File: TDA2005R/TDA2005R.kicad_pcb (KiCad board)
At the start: 2 copper layers, 71.1 x 71.1 mm, 26 parts, among them J1 6-pole_dual_potentiometer_hea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, U1 4-pole_RL-input_screw_terminal, U2 TDA2005, U3 4-pole_RL-output_screw_termin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, U4 2-pole_power_in_screw_terminal

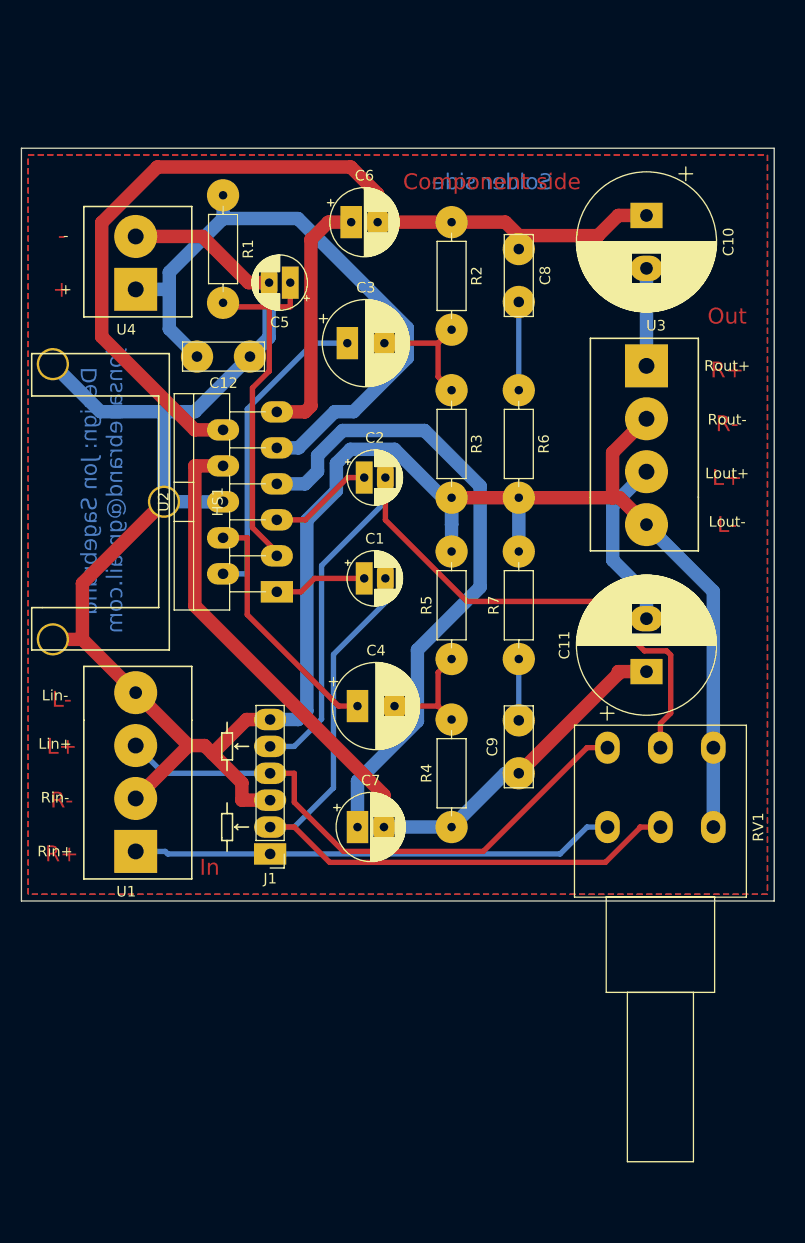
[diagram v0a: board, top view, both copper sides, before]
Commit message: wider tracks and text
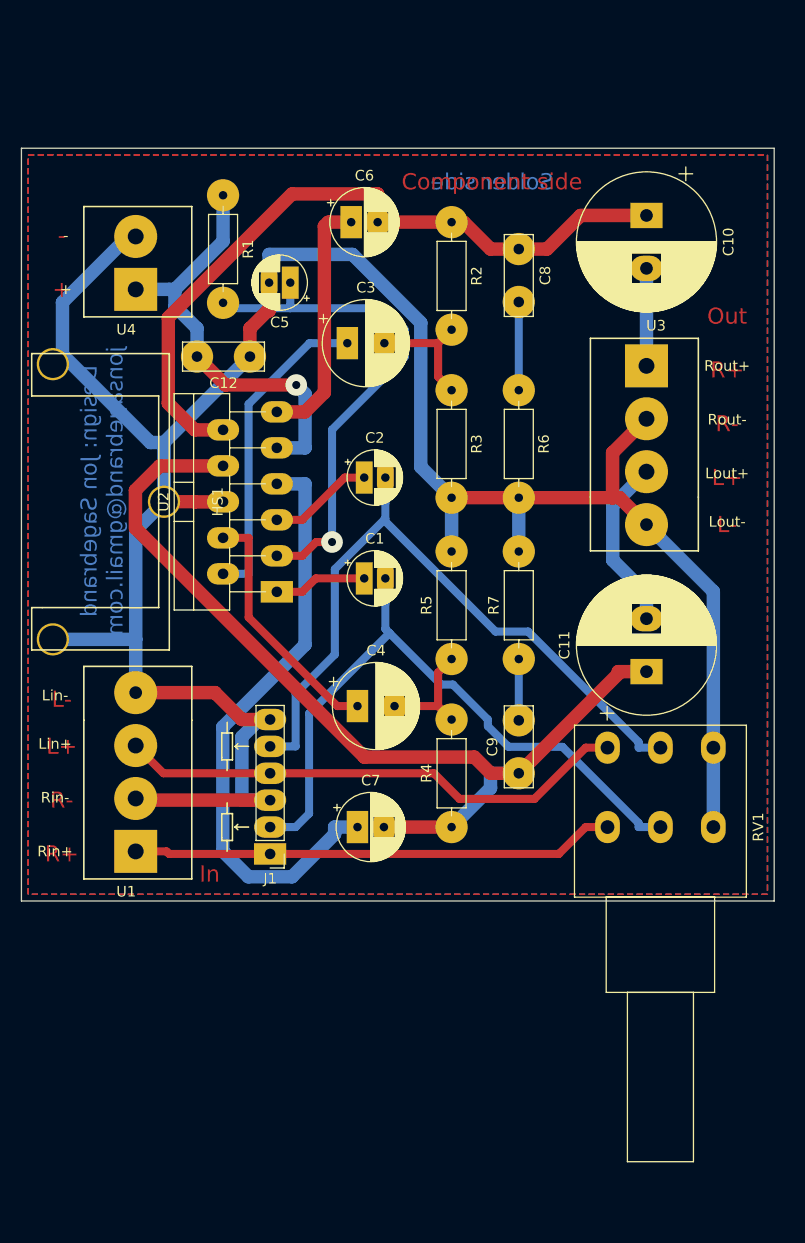
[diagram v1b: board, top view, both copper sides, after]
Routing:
- net +15V: track 62.0 -> 41.1 mm, vias 0 -> 1
- net Net-(C10-Pad1): track 85.8 -> 69.4 mm
- net Net-(C5-Pad1): track 33.9 -> 49.3 mm, vias 0 -> 1
- net Net-(C11-Pad1): track 75.2 -> 90.5 mm
- net Net-(C2-Pad2): track 76.7 -> 66.7 mm
- net Lin: track 54.4 -> 48.7 mm
- net Net-(C1-Pad2): track 69.0 -> 63.5 mm
- net Net-(C7-Pad1): track 61.4 -> 56.7 mm
- net GND: track 230.0 -> 231.7 mm
- added copper zone on B.Cu, net (none)
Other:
- net class 20 removed
- net class 30: via_dia 1.27 -> 2.032
- net class Default: via_dia 0.8 -> 3.048; via_drill 0.4 -> 0.762

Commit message: new component sizes
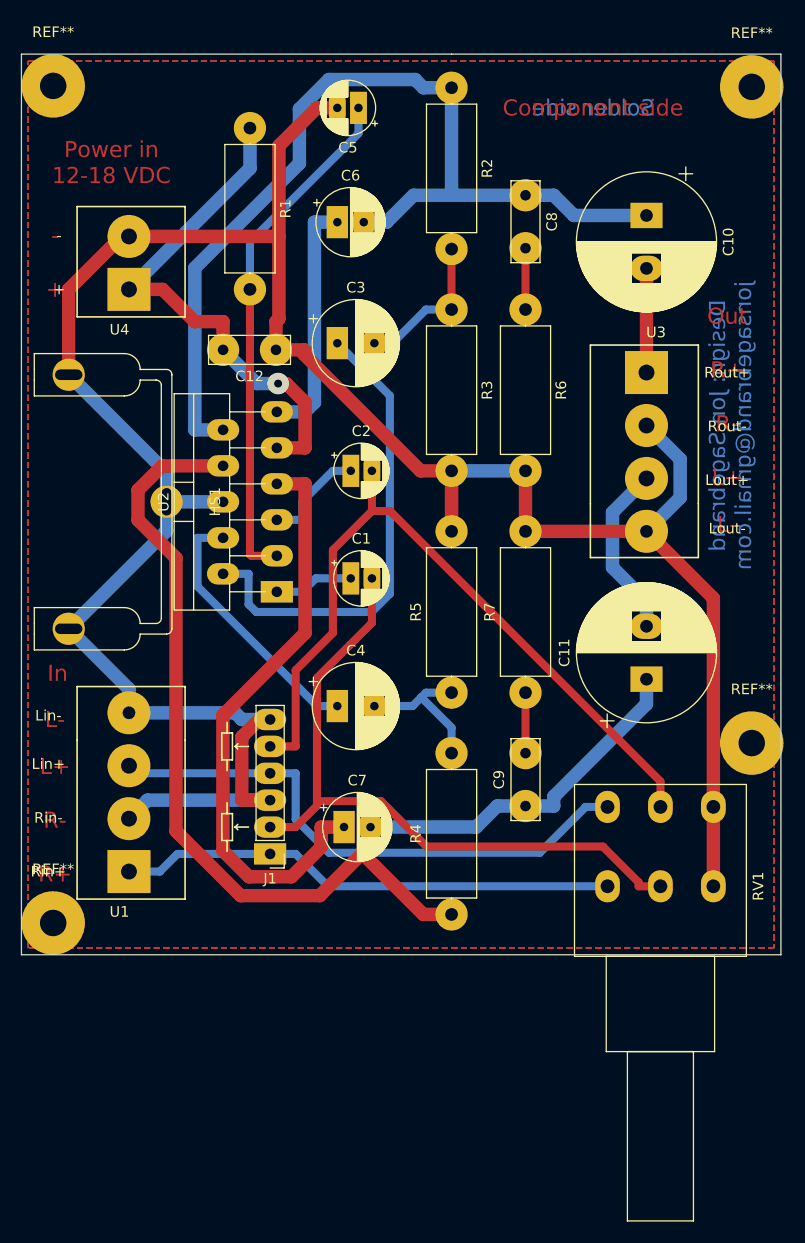
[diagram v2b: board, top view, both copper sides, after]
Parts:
- added REF**: SolderWirePad_1x01_Drill2.5mm, Connector_Wire:SolderWirePad_1x01_Drill2.5mm, F.Cu at (206.2, 119.7)
- added REF**: SolderWirePad_1x01_Drill2.5mm, Connector_Wire:SolderWirePad_1x01_Drill2.5mm, F.Cu at (206.2, 57.7)
- added REF**: SolderWirePad_1x01_Drill2.5mm, Connector_Wire:SolderWirePad_1x01_Drill2.5mm, F.Cu at (140.2, 136.7)
- added REF**: SolderWirePad_1x01_Drill2.5mm, Connector_Wire:SolderWirePad_1x01_Drill2.5mm, F.Cu at (140.2, 57.6)
- R1, R2, R3, R4, R5, R6, R7: footprint My_Misc:R_Axial_DIN0207_L6.3mm_D2.5mm_P10.16mm_Horizontal_larger_pads -> My_Misc:R_Axial_DIN0414_L11.9mm_D4.5mm_P15.24mm_Horizontal_larger
- moved C5 17.7 mm to (169.0, 59.7)
- moved R2 12.7 mm to (177.8, 57.8)
- moved R4 8.25 mm to (177.8, 135.9)
- moved R6 7.65 mm to (184.8, 78.7)
- moved R3 7.62 mm to (177.8, 78.7)
- moved R1 6.84 mm to (158.8, 61.6)
- moved RV1 5.59 mm to (192.5, 133.2)
- moved C8 5.12 mm to (184.8, 67.9)
- moved R7 3.24 mm to (184.8, 114.9)
- moved R5 3.17 mm to (177.8, 114.9)
- moved C9 3.16 mm to (184.8, 125.7)
- moved C12 2.54 mm to (161.2, 82.5)
- moved U1 2.01 mm to (147.3, 131.8)
- moved C4 1.91 mm to (167.0, 116.2)
- moved C2 1.42 mm to (168.3, 94.0)
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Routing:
- net Net-(C10-Pad1): track 69.4 -> 91.6 mm
- net Net-(C11-Pad1): track 90.5 -> 111.9 mm
- net Net-(C3-Pad1): track 30.2 -> 45.4 mm
- net GND: track 231.7 -> 243.6 mm
- net +15V: track 41.1 -> 49.6 mm
- net Net-(C2-Pad2): track 66.7 -> 71.7 mm
- net Lin: track 48.7 -> 53.0 mm
- net Net-(C4-Pad2): track 10.9 -> 14.3 mm
- net Net-(C3-Pad2): track 11.8 -> 14.4 mm
- net Net-(C8-Pad2): track 8.33 -> 5.80 mm
- net Rin: track 45.7 -> 47.2 mm
- net Net-(C1-Pad2): track 63.5 -> 64.9 mm
- net Net-(C1-Pad1): track 8.78 -> 7.51 mm
- net Net-(C4-Pad1): track 23.7 -> 24.9 mm
- net Rout: track 9.21 -> 9.84 mm
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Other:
- board size 71.1 x 71.1 mm -> 71.8 x 85.1 mm
- board text added: "Power in 12-18 VDC"

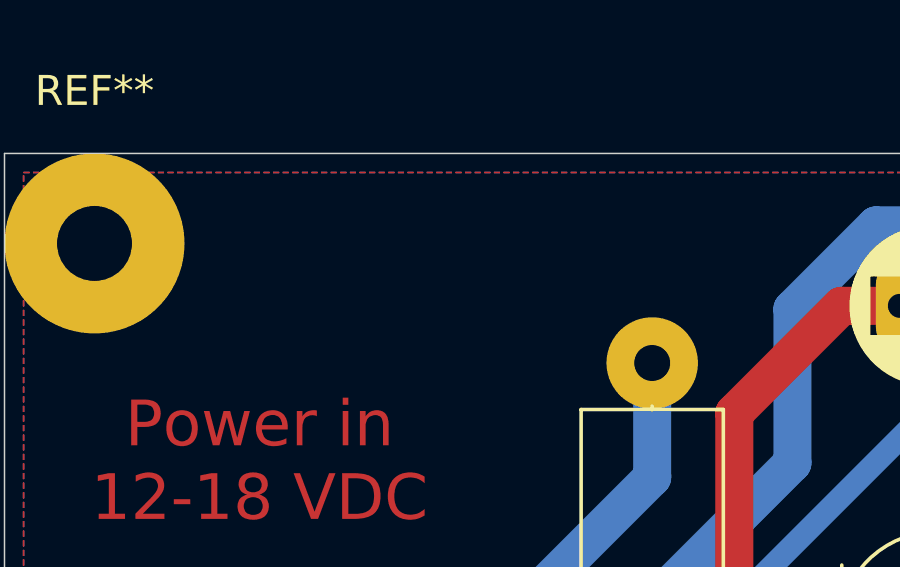
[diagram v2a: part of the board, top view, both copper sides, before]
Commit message: new resistors, new heatsink
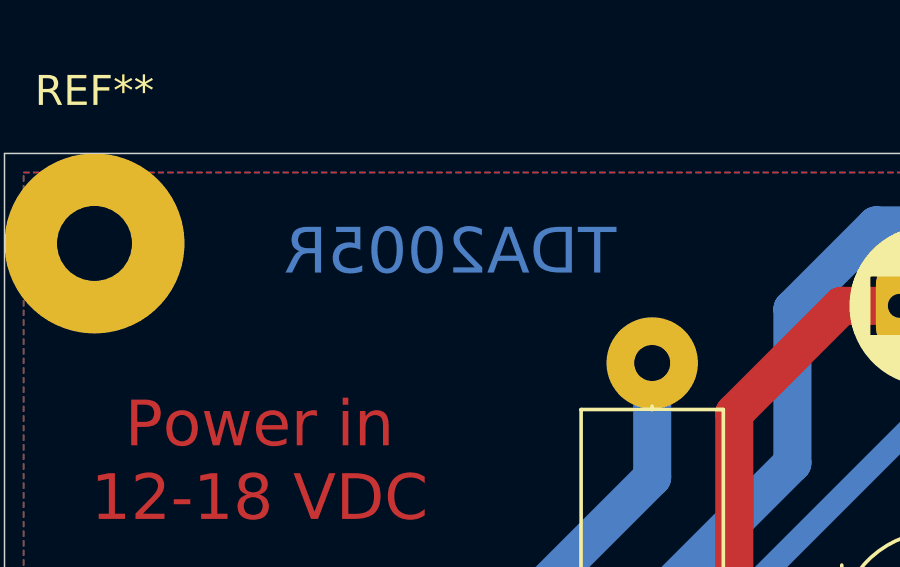
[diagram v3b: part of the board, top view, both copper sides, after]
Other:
- board text added: "TDA2005R"
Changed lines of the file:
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@@
   (general
     (thickness 1.6)
-    (drawings 22)
+    (drawings 23)
     (tracks 182)
     (zones 0)
@@
     )
   )
+  (gr_text TDA2005R (at 152.01 57.875) (layer B.Cu)
+    (effects (font (size 1.524 1.524) (thickness 0.381)) (justify mirror))
+  )
   (gr_text "Power in\n12-18 VDC" (at 145.66 64.86) (layer F.Cu)
